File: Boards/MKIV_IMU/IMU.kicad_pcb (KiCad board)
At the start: 2 copper layers, 50.8 x 55.9 mm, 48 parts, among them J1 UF_8_RA, J4 CONN_02X03, Q1 2N7000, Q2 2N7000, Q3 2N7000, U1 CAN_Transceiver, U2 TPS561201, U3 LM3480, U4 BMI088, U5 ATMEGA16M1, Y1 Crystal_SMD

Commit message: layout rev 3
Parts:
- removed PB5, PB6, PC7: R_200, footprints:R_0805_OEM
- removed Q3: 2N7000, Package_TO_SOT_THT:TO-92_Inline
- added D6: SS110LW, footprints:D_SOD-123W_OEM, F.Cu at (155.8, 86.0)
- added D8: SS110LW, footprints:D_SOD-123W_OEM, F.Cu at (155.6, 83.3)
- added G***: LOGO, footprints:phoenix, B.Cu at (198.8, 95.7)
- added R10: R_200, footprints:R_0805_OEM, F.Cu at (131.3, 79.0)
- added R11: R_200, footprints:R_0805_OEM, F.Cu at (129.9, 80.4)
- added R16: R_10K, footprints:R_0805_OEM, F.Cu at (156.8, 80.2)
- added R6: R_200, footprints:R_0805_OEM, F.Cu at (132.8, 77.5)
- added REF**: Mounting_Hole_4-40, footprints:Mounting_Hole_4-40, F.Cu at (161.9, 75.8)
- added REF**: Mounting_Hole_4-40, footprints:Mounting_Hole_4-40, F.Cu at (161.5, 122.6)
- added REF**: Mounting_Hole_4-40, footprints:Mounting_Hole_4-40, F.Cu at (120.4, 122.4)
- added REF**: Mounting_Hole_4-40, footprints:Mounting_Hole_4-40, F.Cu at (119.8, 75.1)
- C10: value C_0.1uF -> C_1uF
- Q1, Q2: value 2N7000 -> SSM3K333R; footprint Package_TO_SOT_THT:TO-92_Inline -> footprints:SOT-23F
- U3: value LM3480 -> TCR2EF33LM; footprint footprints:SOT-23-3_OEM -> footprints:SOT25
- moved U4 21.1 mm to (154.6, 96.3), turned to 90 degrees
- moved C9 15.6 mm to (106.6, 76.8), turned to 270 degrees
- moved C4 13.2 mm to (121.5, 104.8), turned to 90 degrees
- moved U3 12.4 mm to (109.4, 77.2)
- moved C10 12.3 mm to (112.3, 76.8)
- moved Q1 7.35 mm to (153.2, 75.6), turned to 0 degrees
- moved C13 6.97 mm to (143.6, 78.3), turned to 180 degrees
- moved R13 6.75 mm to (148.6, 75.5)
- moved U1 6.46 mm to (126.4, 103.6), turned to 0 degrees
- moved R15 5.41 mm to (149.7, 84.1), turned to 90 degrees
- moved R7 4.78 mm to (131.4, 103.5), turned to 270 degrees
- moved D2 3.18 mm to (153.9, 100.8)
- moved R9 3.18 mm to (150.9, 104.0)
- moved U2 3.18 mm to (151.0, 117.0)
- moved C11 3.18 mm to (157.9, 109.7)
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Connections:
- C9 pad 1: VCC -> Net-(C9-Pad1)
- Q1 pad 1: /MOSI2 -> Net-(Q1-Pad1)
- Q1 pad 2: Net-(Q1-Pad2) -> GND
- Q1 pad 3: GND -> /MOSI2
- Q2 pad 1: /SCK2 -> Net-(Q2-Pad1)
- Q2 pad 2: Net-(Q2-Pad2) -> GND
- Q2 pad 3: GND -> /SCK2
- R13 pad 1: Net-(Q1-Pad2) -> Net-(Q1-Pad1)
- R14 pad 1: Net-(Q2-Pad2) -> Net-(Q2-Pad1)
- R15 pad 1: Net-(R15-Pad1) -> VCC
- R15 pad 2: Net-(Q3-Pad2) -> Net-(D8-Pad2)
- U3 pad 1: /3.3V -> Net-(C9-Pad1)
- U3 pad 2: VCC -> GND
- U3 pad 3: GND -> Net-(C9-Pad1)
- U4 pad 10: Net-(R15-Pad1) -> /MISO2
- U4 pad 14: /CS_ACCEL -> Net-(D6-Pad2)
- U4 pad 15: Net-(R15-Pad1) -> /MISO2
- U4 pad 5: /CS_GYRO -> Net-(D8-Pad2)
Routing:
- net VCC: track 96.9 -> 34.7 mm
- net /3.3V: track 45.8 -> 1.84 mm, vias 3 -> 0
- net /MOSI2: track 28.5 -> 0.00 mm, vias 1 -> 0
- net /MISO2: track 19.3 -> 0.00 mm, vias 1 -> 0
- net /CS_ACCEL: track 15.3 -> 0.00 mm
- net /INT1: track 14.8 -> 0.00 mm, vias 2 -> 0
- net GND: track 51.4 -> 36.9 mm, vias 28 -> 23
- net /RXCAN: track 14.4 -> 0.00 mm
- net /SCK2: track 11.1 -> 0.00 mm, vias 1 -> 0
- net /INT4: track 9.87 -> 0.00 mm
- net Net-(R13-Pad2): track 9.39 -> 0.00 mm
- net Net-(R15-Pad1): track 9.16 -> 0.00 mm
- net /TXCAN: track 9.10 -> 0.00 mm
- net /CS_GYRO: track 6.42 -> 0.00 mm
- net Net-(Q3-Pad2): track 5.33 -> 0.00 mm
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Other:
- board text added: "OEM COM Board Dhara Patel rev. 3"
- board text removed: "OEM COM Board Dhara Patel rev. 2"
- board text removed: "x"
- board text removed: "y"

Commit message: IMU rev 3
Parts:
- moved Q1 20.8 mm to (153.0, 96.5), turned to 270 degrees
- moved C13 19.1 mm to (124.6, 76.4)
- moved R13 18.1 mm to (153.9, 92.7), turned to 90 degrees
- moved U4 16.3 mm to (153.4, 80.1), turned to 0 degrees
- moved D8 12.7 mm to (143.7, 79.1), turned to 45 degrees
- moved C9 11.3 mm to (117.2, 80.9)
- moved C10 11.3 mm to (122.9, 80.9)
- moved U3 11.3 mm to (120.0, 81.3)
- moved R16 8.90 mm to (150.7, 86.6), turned to 180 degrees
- moved G*** 7.23 mm to (205.5, 98.5)
- moved D6 6.56 mm to (150.0, 89.0)
- moved R15 5.68 mm to (147.7, 78.8)
- moved R11 5.40 mm to (130.1, 75.0), turned to 90 degrees
- moved D5 4.94 mm to (130.1, 78.8), turned to 270 degrees
- moved R8 4.77 mm to (127.1, 83.3), turned to 0 degrees
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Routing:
- net VCC: track 34.7 -> 95.5 mm, vias 0 -> 1
- net /3.3V: track 1.84 -> 52.6 mm, vias 0 -> 4
- net /MISO2: track 0.00 -> 26.9 mm, vias 0 -> 3
- net /INT4: track 0.00 -> 25.5 mm
- net /RXCAN: track 0.00 -> 18.8 mm
- net /MOSI2: track 0.00 -> 17.8 mm
- net /TXCAN: track 0.00 -> 16.7 mm
- net GND: track 36.9 -> 53.3 mm, vias 23 -> 28
- net Net-(R14-Pad2): track 0.00 -> 14.8 mm
- net /SCK2: track 0.00 -> 11.9 mm
- net /INT1: track 0.00 -> 11.5 mm, vias 0 -> 2
- net Net-(R13-Pad2): track 0.00 -> 10.6 mm
- net Net-(D8-Pad2): track 0.00 -> 10.2 mm
- net Net-(D6-Pad2): track 0.00 -> 8.17 mm
- net /PLED3: track 3.28 -> 8.63 mm
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
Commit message: this is real i think
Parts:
- moved C9 43.1 mm to (159.6, 88.3), turned to 0 degrees
- moved U3 40.1 mm to (159.9, 85.4), turned to 0 degrees
- moved C10 36.7 mm to (159.6, 82.5), turned to 0 degrees
- moved C13 27.7 mm to (152.3, 75.0)
- moved C14 10.7 mm to (152.3, 76.5), turned to 0 degrees
- moved R1 2.82 mm to (144.9, 82.4), turned to 135 degrees
- moved D8 1.46 mm to (142.4, 79.9)
- moved C2 1.06 mm to (143.4, 83.7), turned to 135 degrees
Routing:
- net GND: track 53.3 -> 231.3 mm, vias 28 -> 47
- net /3.3V: track 52.6 -> 16.7 mm, vias 4 -> 0
- net VCC: track 95.5 -> 70.6 mm, vias 1 -> 2
- net Net-(R14-Pad2): track 14.8 -> 0.00 mm
- net /INT4: track 25.5 -> 20.5 mm
- net /CS_GYRO: track 4.80 -> 3.52 mm
- net Net-(D8-Pad2): track 10.2 -> 9.10 mm, vias 0 -> 2
- net /INT1: track 11.5 -> 10.6 mm, vias 2 -> 0
- net Net-(C2-Pad1): track 4.33 -> 5.12 mm
- net /MISO2: track 26.9 -> 27.1 mm, vias 3 -> 4
- added copper zone on F.Cu, net (none)
- removed copper zone on F.Cu, net VCC

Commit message: rev 3 changes!
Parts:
- moved R16 1.84 mm to (152.5, 86.5), turned to 0 degrees
- moved R15 0.47 mm to (147.5, 79.2)
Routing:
- net Net-(R14-Pad2): track 0.00 -> 21.4 mm
- net VCC: track 70.6 -> 90.6 mm, vias 2 -> 4
- net GND: track 231.3 -> 236.5 mm, vias 47 -> 49
- net Net-(D8-Pad2): track 9.10 -> 13.0 mm
- net Net-(C8-Pad1): track 4.04 -> 5.99 mm

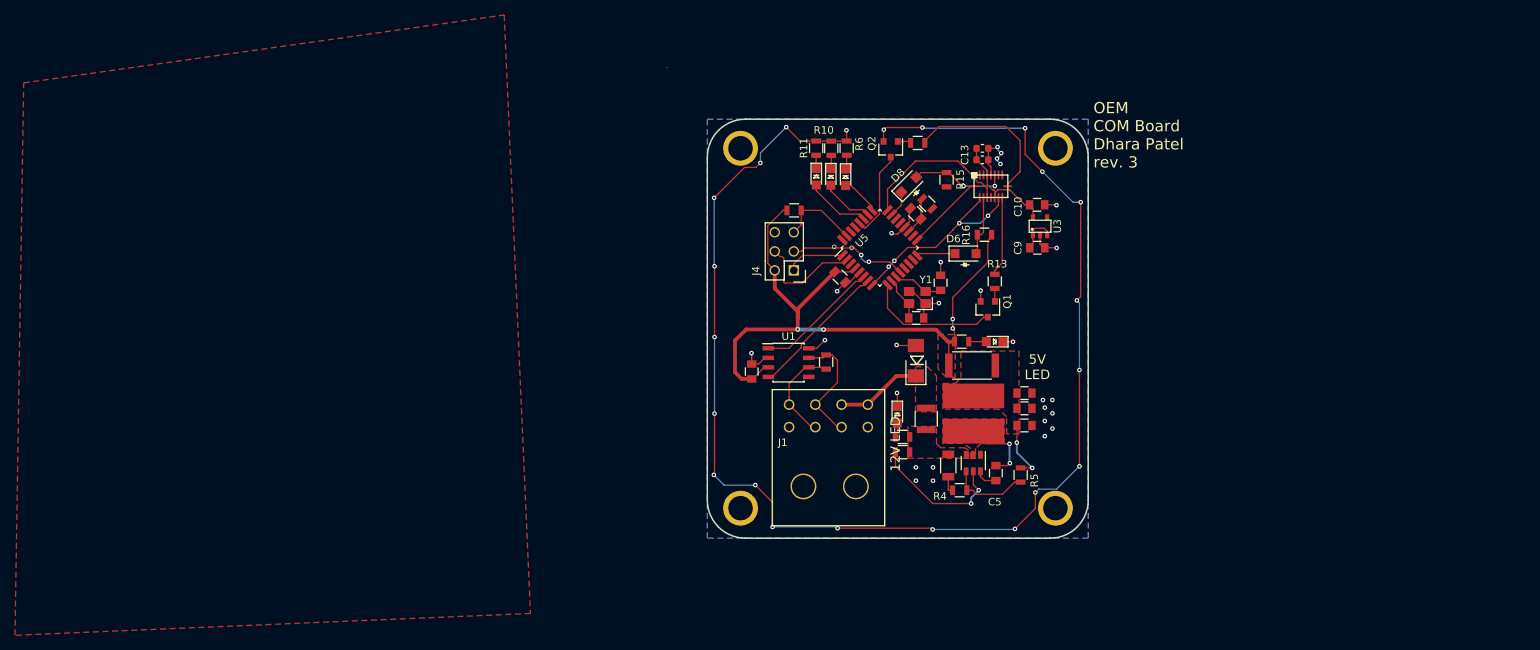
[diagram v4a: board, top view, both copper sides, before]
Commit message: Complete rev 3 of COM board; needs review and final check off
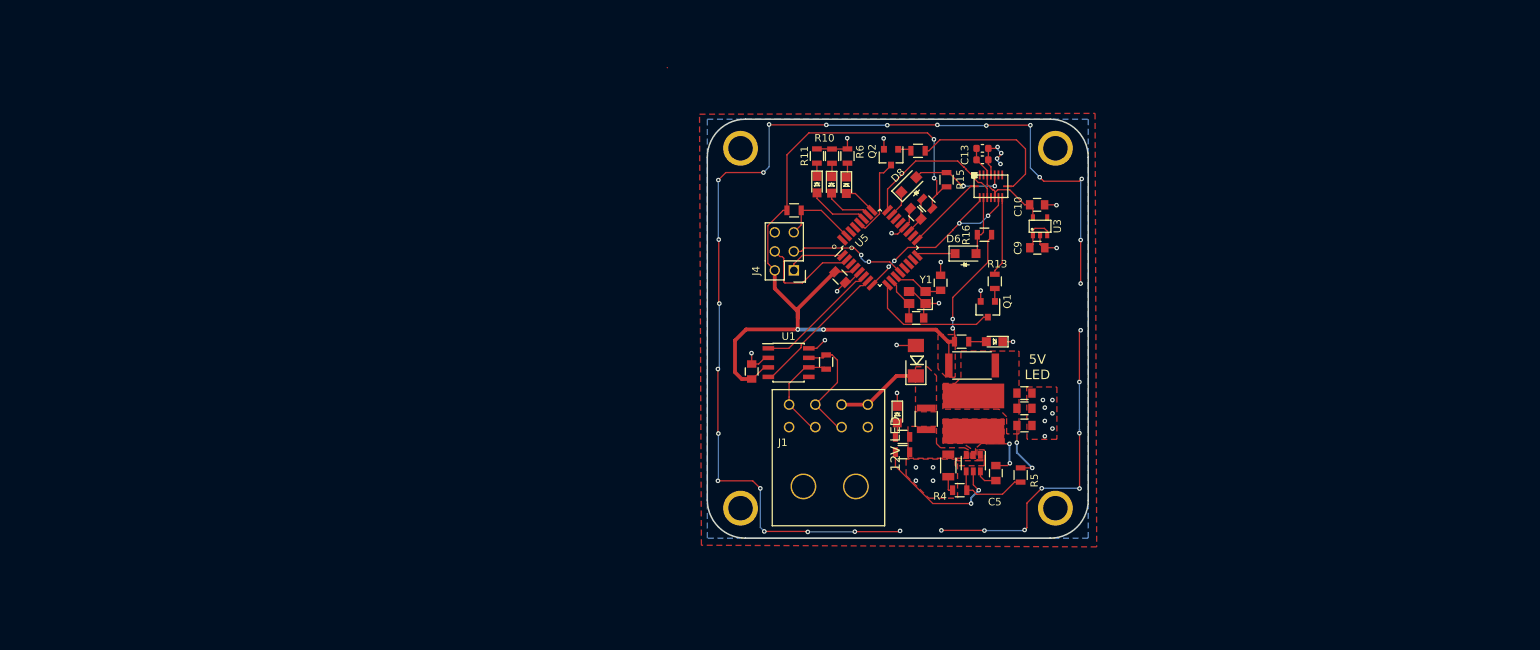
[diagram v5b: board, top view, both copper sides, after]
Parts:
- moved G*** 60.7 mm to (145.7, 108.5), turned to 180 degrees
- moved D3 1.06 mm to (134.1, 79.9)
- moved R6 1.06 mm to (134.3, 76.0)
- moved R10 1.06 mm to (132.2, 76.0)
- moved D4 1.06 mm to (132.1, 79.9)
- moved D5 1.06 mm to (130.2, 79.8)
- moved R11 1.06 mm to (130.2, 76.0)
- moved Q2 1.05 mm to (140.1, 76.2)
- moved R14 1.05 mm to (143.7, 75.3)
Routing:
- net VCC: track 90.6 -> 130.6 mm, vias 4 -> 6
- net GND: track 236.5 -> 243.8 mm, vias 49 -> 59
- net /PLED1: track 5.21 -> 4.37 mm
- net /SCK2: track 11.9 -> 11.2 mm
- net /PLED3: track 8.63 -> 8.09 mm
- net /PLED2: track 7.01 -> 6.47 mm

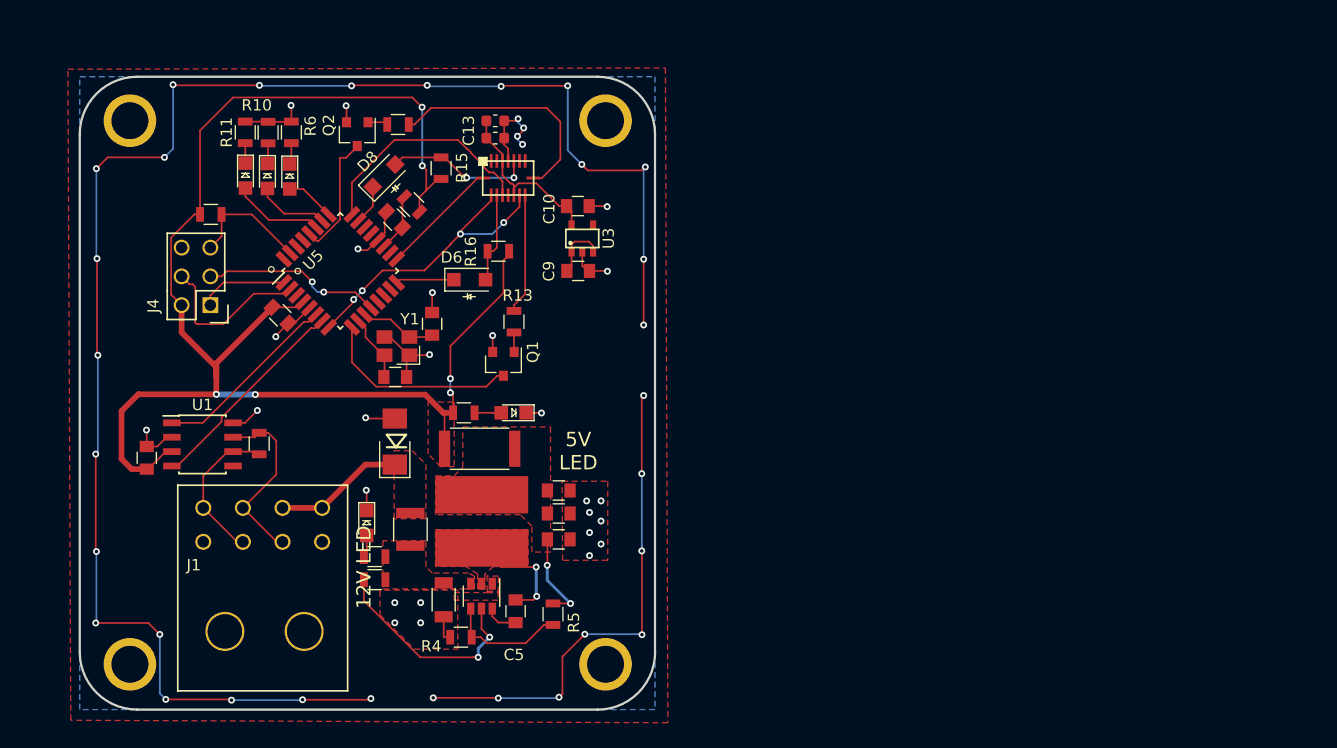
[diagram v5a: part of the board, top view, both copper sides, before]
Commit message: fixed fets on schematic
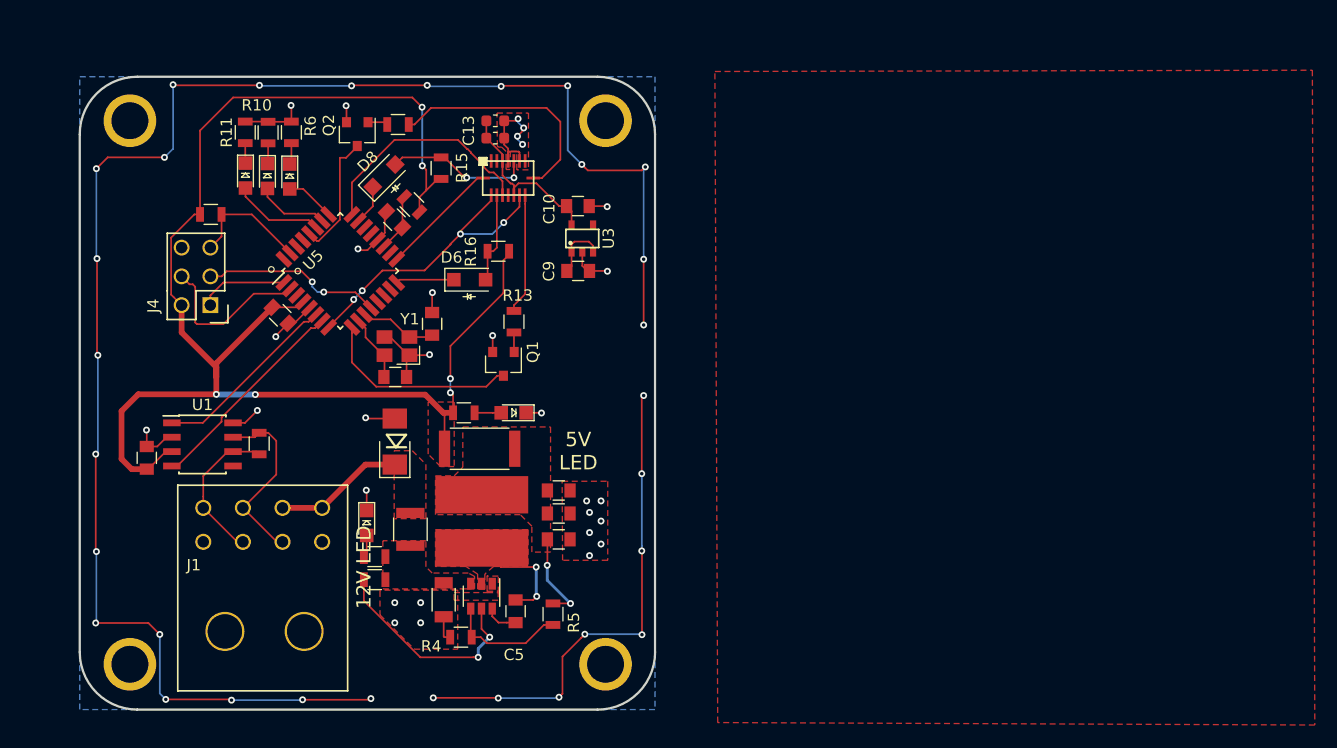
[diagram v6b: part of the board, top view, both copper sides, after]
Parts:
- moved G*** 61.9 mm to (83.8, 105.7)
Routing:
- net GND: track 243.8 -> 246.9 mm
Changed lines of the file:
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@@
     (thickness 1.6)
     (drawings 12)
-    (tracks 481)
+    (tracks 487)
     (zones 0)
     (modules 55)
@@
   )
   (module footprints:phoenix (layer B.Cu)
-    (at 145.67916 108.5342 180)
+    (at 83.8454 105.73512 180)
     (fp_text reference G*** (at 0 0 180) (layer B.SilkS) hide
       (effects (font (size 1.524 1.524) (thickness 0.3)) (justify mirror))
@@
   (segment (start 135.20928 126.16688) (end 135.24484 126.13132) (width 0.1524) (layer B.Cu) (net 1))
   (segment (start 128.97104 126.16688) (end 135.20928 126.16688) (width 0.1524) (layer B.Cu) (net 1))
+  (segment (start 154.324559 77.727279) (end 154.40076 77.80348) (width 0.1524) (layer F.Cu) (net 1))
+  (segment (start 153.476961 77.727279) (end 154.324559 77.727279) (width 0.1524) (layer F.Cu) (net 1))
+  (segment (start 153.40076 77.80348) (end 153.476961 77.727279) (width 0.1524) (layer F.Cu) (net 1))
+  (segment (start 154.40076 77.80348) (end 154.40076 78.55588) (width 0.1524) (layer F.Cu) (net 1))
+  (segment (start 153.40076 78.55588) (end 153.40076 77.80348) (width 0.1524) (layer F.Cu) (net 1))
+  (segment (start 154.40076 78.55588) (end 154.90076 78.55588) (width 0.1524) (layer F.Cu) (net 1))
   (segment (start 134.795368 91.479653) (end 135.28981 90.985211) (width 0.1524) (layer F.Cu) (net 2))
   (segment (start 132.566693 91.479653) (end 134.795368 91.479653) (width 0.1524) (layer F.Cu) (net 2))
@@
     (polygon
       (pts
-        (xy 167.50284 128.16332) (xy 114.77752 127.94488) (xy 114.5286 70.45452) (xy 167.2844 70.34276)
+        (xy 224.629233 128.364071) (xy 171.903913 128.145631) (xy 171.654993 70.655271) (xy 224.410793 70.543511)
       )
     )
@@
       )
     )
+  )
+  (zone (net 1) (net_name GND) (layer F.Cu) (hatch edge 0.508)
+    (connect_pads (clearance 0.1524))
+    (min_thickness 0.254)
+    (fill yes (arc_segments 16) (thermal_gap 0.508) (thermal_bridge_width 0.508))
+    (polygon
+      (pts
+        (xy 152.41016 74.32548) (xy 155.194 74.32548) (xy 155.194 79.33944) (xy 154.16276 79.33944) (xy 154.16276 77.6986)
+        (xy 153.58364 77.6986) (xy 153.58364 79.30896) (xy 153.29408 79.30896) (xy 153.21788 79.30896) (xy 153.21788 77.71892)
+        (xy 152.8318 77.33284) (xy 152.53208 77.33284) (xy 152.4508 77.25156)
+      )
+    )
